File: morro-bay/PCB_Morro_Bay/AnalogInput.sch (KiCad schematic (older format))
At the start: 117 parts, among them SW1 SW_DIP_x10, SW2 SW_DIP_x10, U10 LM2902, U11 LM2902, U12 LM2902, U5 LM2902, U6 LM2902, U7 LM2902, U8 LM2902, U9 LM2902

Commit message: Even more BOM and footprints
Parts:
- added C32, C66: 22uF, Capacitor_SMD:C_0805_2012Metric_Pad1.15x1.40mm_HandSolder, symbol Device:C
- R10, R12, R14, R16, R22, R24, R26, R28, R34, R36, R38, R40, R46, R48, R50, R52, R58, R60, R64, R66: footprint (none) -> Resistor_SMD:R_0603_1608Metric_Pad1.05x0.95mm_HandSolder; Digikey (none) -> https://www.digikey.ca/product-detail/en/panasonic-electron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; Part Number (none) -> ERJ-PB3B1003V
- R11, R13, R15, R21, R23, R25, R27, R33, R35, R9: footprint (none) -> Resistor_SMD:R_0603_1608Metric_Pad1.05x0.95mm_HandSolder; Digikey (none) -> https://www.digikey.ca/product-detail/en/panasonic-electron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; Part Number (none) -> ERJ-PB3B5112V
- R17, R18, R19, R20, R29, R30, R31, R32, R41, R42, R43, R44, R53, R54, R55, R56, R61, R62, R67, R68: value 500 -> 470; footprint (none) -> Resistor_SMD:R_0603_1608Metric_Pad1.05x0.95mm_HandSolder; Digikey (none) -> https://www.digikey.ca/product-detail/en/stackpole-electron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; Part Number (none) -> RMCF0603FT470R
- R37, R39, R45, R47: value 205K -> 51.1K; footprint (none) -> Resistor_SMD:R_0603_1608Metric_Pad1.05x0.95mm_HandSolder; Digikey (none) -> https://www.digikey.ca/product-detail/en/panasonic-electron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; Part Number (none) -> ERJ-PB3B5112V
- R49, R51: footprint (none) -> Resistor_SMD:R_0603_1608Metric_Pad1.05x0.95mm_HandSolder; Digikey (none) -> https://www.digikey.ca/product-detail/en/panasonic-electron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; Part Number (none) -> ERA-3AEB2053V
- R57, R59, R63, R65: value 51.1K -> 205K; footprint (none) -> Resistor_SMD:R_0603_1608Metric_Pad1.05x0.95mm_HandSolder; Digikey (none) -> https://www.digikey.ca/product-detail/en/panasonic-electron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; Part Number (none) -> ERA-3AEB2053V
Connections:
- net 5V_IN_15 is gone; now on net 10V_IN_1: SW2.5
- net 5V_IN_16 is gone; now on net 10V_IN_2: SW2.6
- net 5V_IN_17 is gone; now on net 10V_IN_3: R57.1, SW2.7
- net 5V_IN_20 is gone; now on net 10V_IN_6: R65.1, SW2.10
- net 10V_IN_1: now also R49.1; no longer R37.1
- net 10V_IN_2: now also R51.1; no longer R39.1
- net 10V_IN_3: no longer R45.1
- net 10V_IN_4: now also R59.1, SW2.8; no longer R47.1
- net 10V_IN_5: now also R63.1, SW2.9; no longer R49.1
- net 10V_IN_6: no longer R51.1
- net 3V3_IN_18: now also R59.2, R60.1; no longer R63.2, R64.1
- net 3V3_IN_19: now also R63.2, R64.1; no longer R59.2, R60.1
- net 5V_IN_11: now also R37.1
- net 5V_IN_12: now also R39.1
- net 5V_IN_13: now also R45.1
- net 5V_IN_14: now also R47.1
- net GND: now also C32.2, C66.2
- net IN_18_BUFFERED: now also R62.2; no longer R67.2
- net IN_19_BUFFERED: now also R67.2; no longer R62.2
- net SAMD_ADC_18: now also R62.1; no longer R67.1
- net SAMD_ADC_19: now also R67.1; no longer R62.1
- removed net 5V_IN_18: R63.1, SW2.8
- removed net 5V_IN_19: R59.1, SW2.9
- new net +3V3: C32.1, C66.1
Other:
- moved on the sheet: C40, C41

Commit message: BOM BOM BOM BOM baBOM BOM baBOM...
(Imperial march)
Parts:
- SW1, SW2: footprint (none) -> Button_Switch_SMD:SW_DIP_SPSTx10_Slide_6.7x26.96mm_W8.61mm_P2.54mm_LowProfile; Digikey (none) -> https://www.digikey.ca/product-detail/en/cui-devices/DS04-2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; Part Number (none) -> DS04-254-2-10BK-SMT
- U5, U6, U7, U8, U9: footprint (none) -> Package_SO:SOIC-14_3.9x8.7mm_P1.27mm
- U5, U6, U7, U8, U9: footprint (none) -> Package_SO:SOIC-14_3.9x8.7mm_P1.27mm; Digikey (none) -> https://www.digikey.ca/product-detail/en/texas-instruments/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; Part Number (none) -> LM2902LVIDR
- U9: renamed from U11; footprint (none) -> Package_SO:SOIC-14_3.9x8.7mm_P1.27mm
- U9: renamed from U10; footprint (none) -> Package_SO:SOIC-14_3.9x8.7mm_P1.27mm
- U9: renamed from U12; footprint (none) -> Package_SO:SOIC-14_3.9x8.7mm_P1.27mm
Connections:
- net 3V3_IN_18: now also U9.5 (+); no longer U9.3 (+)
- net 3V3_IN_19: now also U9.10 (+); no longer U9.3 (+)
- net 3V3_IN_20: now also U9.12 (+); no longer U9.3 (+)
- net IN_18_BUFFERED: now also U9.6 (-), U9.7; no longer U9.1, U9.2 (-)
- net IN_19_BUFFERED: now also U9.8, U9.9 (-); no longer U9.1, U9.2 (-)
- net IN_20_BUFFERED: now also U9.13 (-), U9.14; no longer U9.1, U9.2 (-)

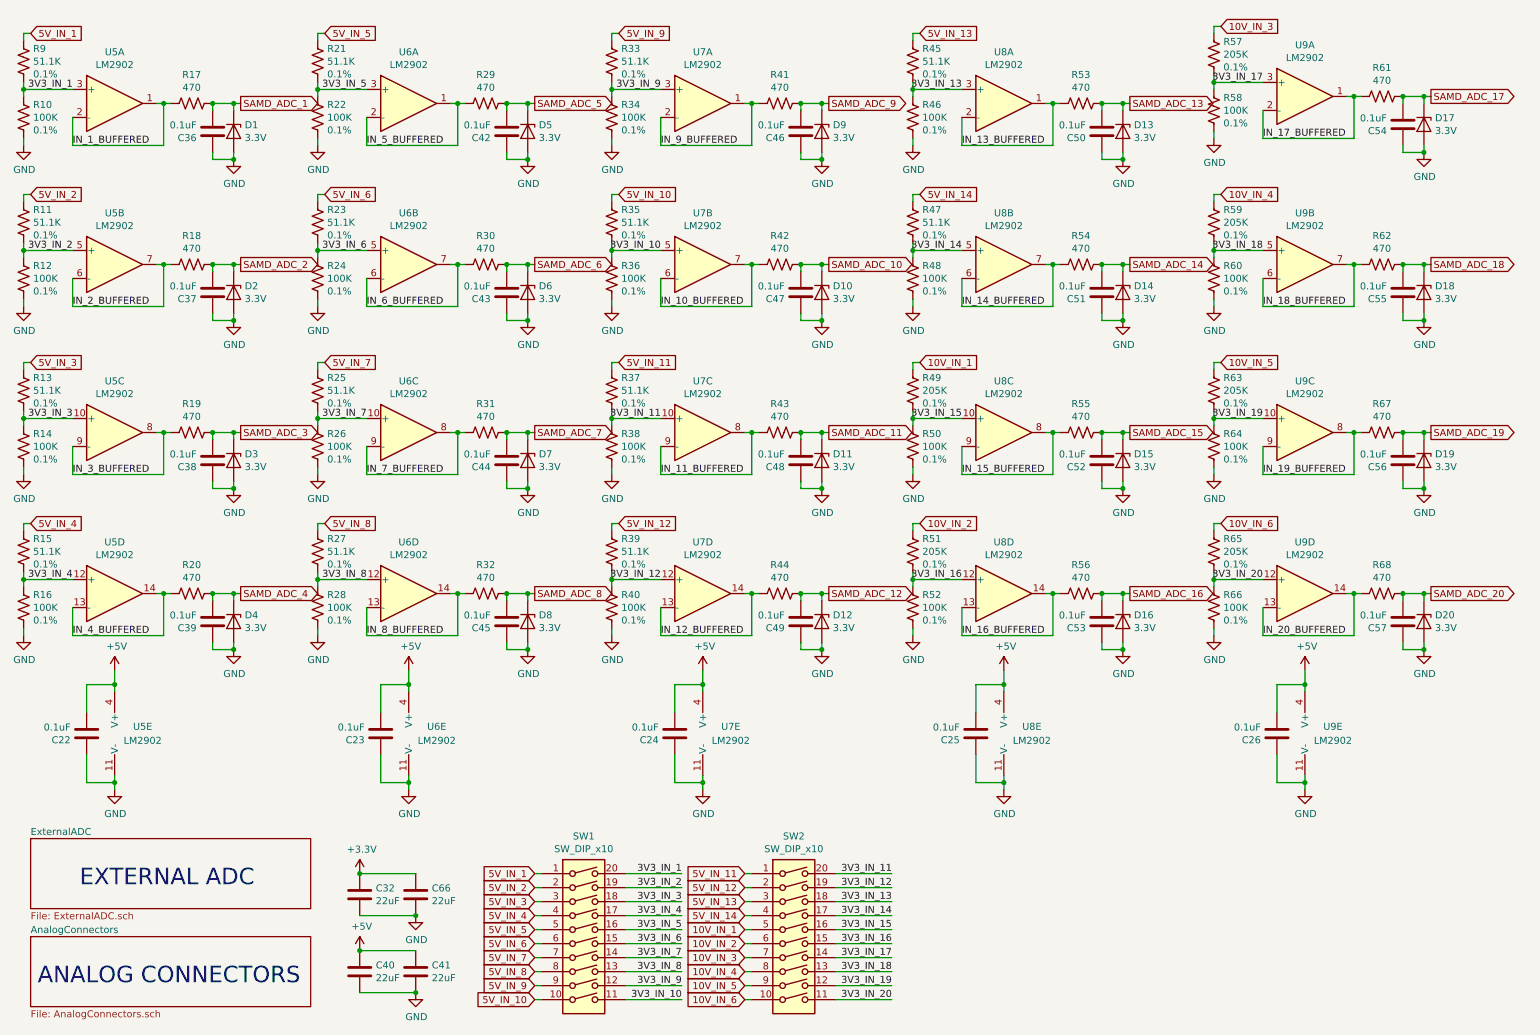
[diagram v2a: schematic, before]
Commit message: Start layout, finish BOM
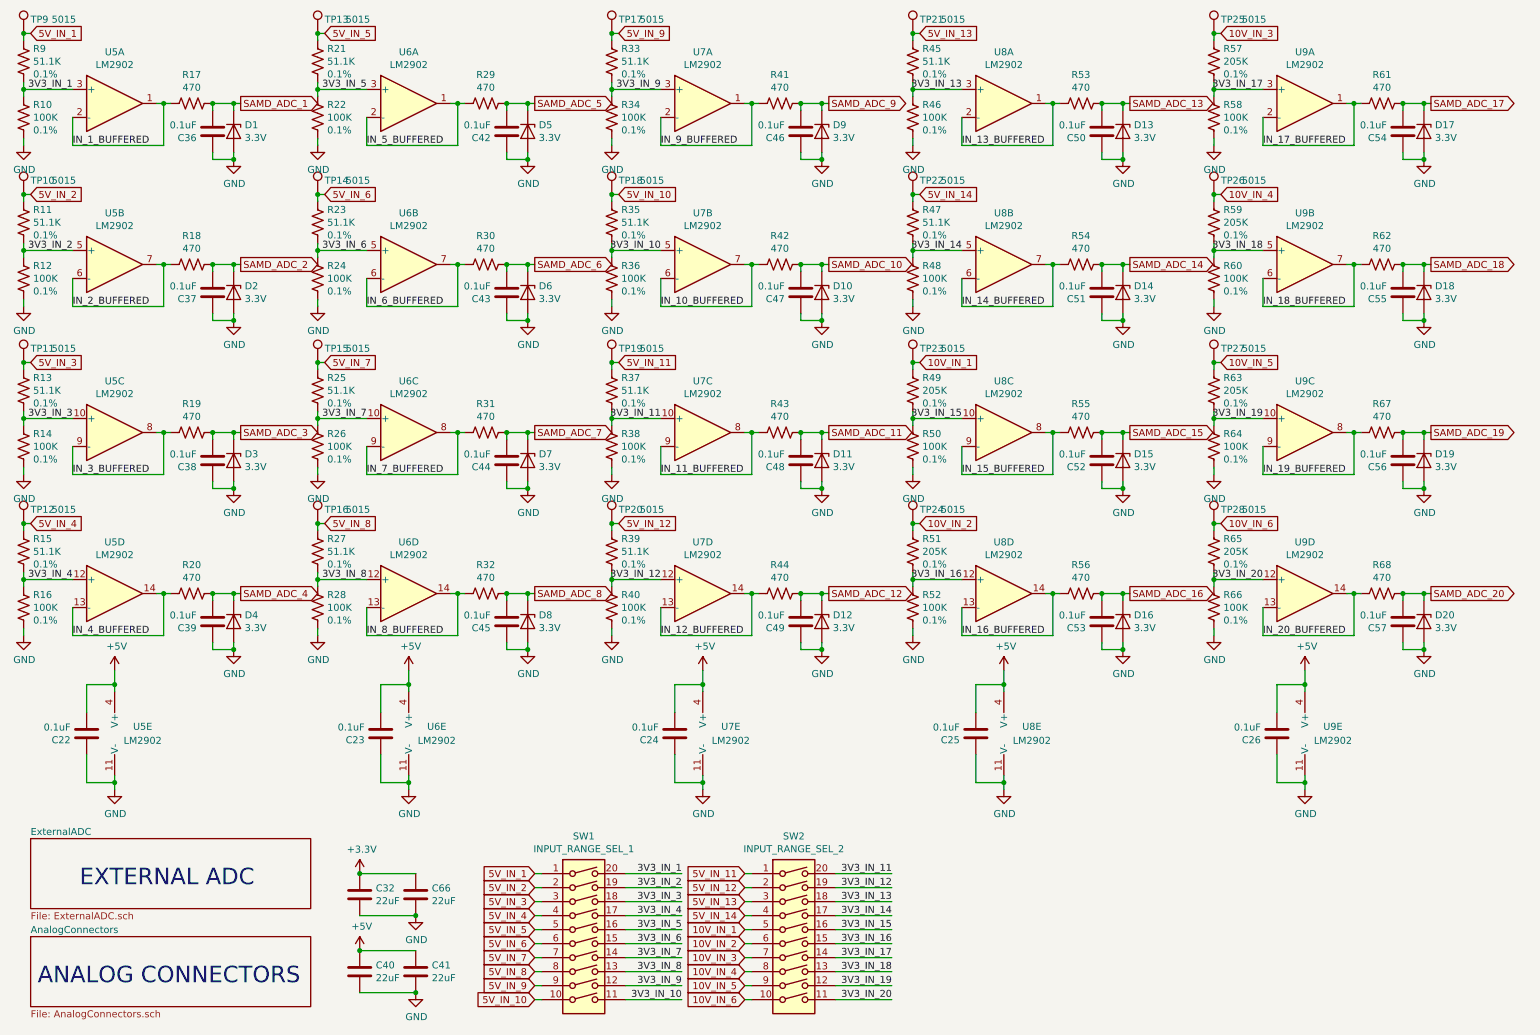
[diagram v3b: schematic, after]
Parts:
- added TP10, TP11, TP12, TP13, TP14, TP15, TP16, TP17, TP18, TP19, TP20, TP21, TP22, TP23, TP24, TP25, TP26, TP27, TP28, TP9: 5015, TestPoint:TestPoint_Keystone_5015_Micro-Minature, symbol Connector:TestPoint
- SW1: value SW_DIP_x10 -> INPUT_RANGE_SEL_1
- SW2: value SW_DIP_x10 -> INPUT_RANGE_SEL_2
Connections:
- net 10V_IN_1: now also TP23.1
- net 10V_IN_2: now also TP24.1
- net 10V_IN_3: now also TP25.1
- net 10V_IN_4: now also TP26.1
- net 10V_IN_5: now also TP27.1
- net 10V_IN_6: now also TP28.1
- net 5V_IN_1: now also TP9.1
- net 5V_IN_10: now also TP18.1
- net 5V_IN_11: now also TP19.1
- net 5V_IN_12: now also TP20.1
- net 5V_IN_13: now also TP21.1
- net 5V_IN_14: now also TP22.1
- net 5V_IN_2: now also TP10.1
- net 5V_IN_3: now also TP11.1
- net 5V_IN_4: now also TP12.1
- net 5V_IN_5: now also TP13.1
- net 5V_IN_6: now also TP14.1
- net 5V_IN_7: now also TP15.1
- net 5V_IN_8: now also TP16.1
- net 5V_IN_9: now also TP17.1
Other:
- moved on the sheet: C54, D17, R57, R58, R61, U9A

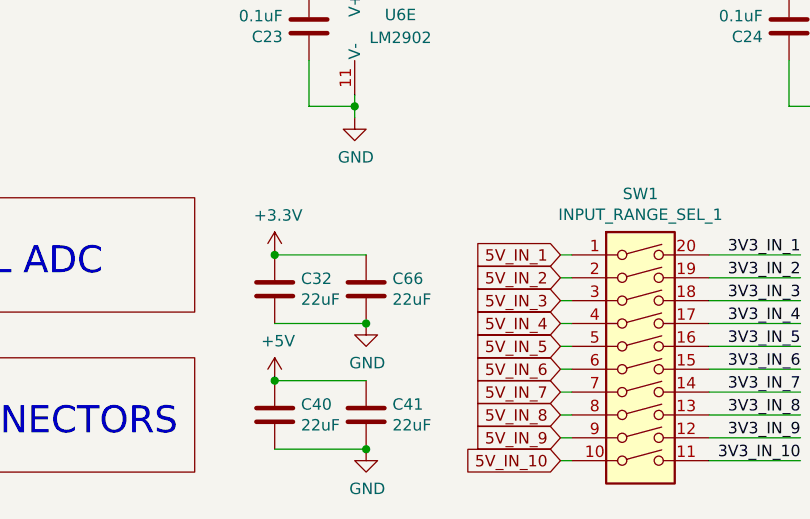
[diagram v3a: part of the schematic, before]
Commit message: Fix values of C7 and C8
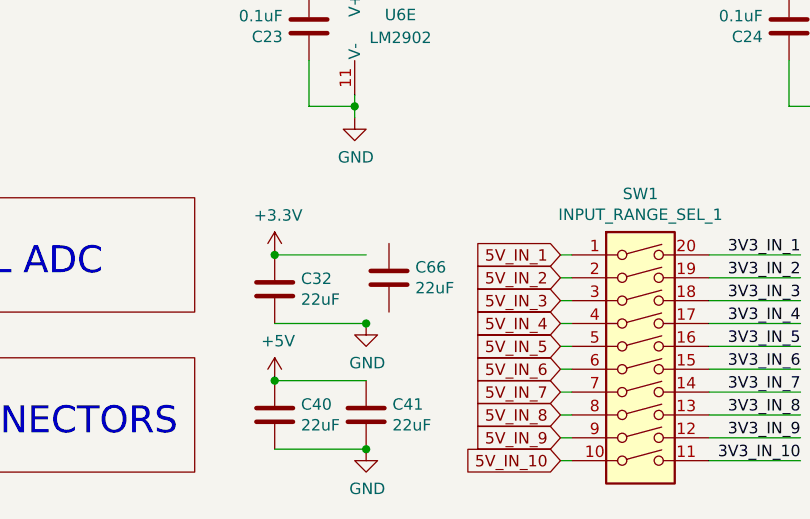
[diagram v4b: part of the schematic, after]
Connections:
- net +3V3: no longer C66.1
- net GND: no longer C66.2
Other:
- moved on the sheet: C66
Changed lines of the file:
@@
 L Device:C C?
 U 1 1 5E88C60F
-P 3400 6800
+P 3500 6750
 AR Path="/5E88C60F" Ref="C?"  Part="1"
 AR Path="/5E59A680/5E88C60F" Ref="C66"  Part="1"
-F 0 "C66" H 3515 6846 50  0000 L CNN
-F 1 "22uF" H 3515 6755 50  0000 L CNN
-F 2 "Capacitor_SMD:C_0805_2012Metric_Pad1.15x1.40mm_HandSolder" H 3438 6650 50  0001 C CNN
-F 3 "~" H 3400 6800 50  0001 C CNN
-F 4 "CL21A226MAQNNNE" H 3400 6800 50  0001 C CNN "Part Number"
-F 5 "https://www.digikey.ca/product-detail/en/samsung-electro-mechanics/CL21A226MAQNNNE/1276-2908-1-ND/3890994" H 3400 6800 50  0001 C CNN "Digikey"
-	1    3400 6800
+F 0 "C66" H 3615 6796 50  0000 L CNN
+F 1 "22uF" H 3615 6705 50  0000 L CNN
+F 2 "Capacitor_SMD:C_0805_2012Metric_Pad1.15x1.40mm_HandSolder" H 3538 6600 50  0001 C CNN
+F 3 "~" H 3500 6750 50  0001 C CNN
+F 4 "CL21A226MAQNNNE" H 3500 6750 50  0001 C CNN "Part Number"
+F 5 "https://www.digikey.ca/product-detail/en/samsung-electro-mechanics/CL21A226MAQNNNE/1276-2908-1-ND/3890994" H 3500 6750 50  0001 C CNN "Digikey"
+	1    3500 6750
 	1    0    0    -1
 $EndComp

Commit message: Start routing
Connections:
- net +3V3: now also C66.1
- net GND: now also C66.2
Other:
- moved on the sheet: C66
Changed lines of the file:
@@
 Wire Wire Line
 	3000 6950 3400 6950
-Connection ~ 3400 6950
 $Comp
 L Device:C C?
@@
 L Device:C C?
 U 1 1 5E88C60F
-P 3500 6750
+P 3400 6800
 AR Path="/5E88C60F" Ref="C?"  Part="1"
 AR Path="/5E59A680/5E88C60F" Ref="C66"  Part="1"
-F 0 "C66" H 3615 6796 50  0000 L CNN
-F 1 "22uF" H 3615 6705 50  0000 L CNN
-F 2 "Capacitor_SMD:C_0805_2012Metric_Pad1.15x1.40mm_HandSolder" H 3538 6600 50  0001 C CNN
-F 3 "~" H 3500 6750 50  0001 C CNN
-F 4 "CL21A226MAQNNNE" H 3500 6750 50  0001 C CNN "Part Number"
-F 5 "https://www.digikey.ca/product-detail/en/samsung-electro-mechanics/CL21A226MAQNNNE/1276-2908-1-ND/3890994" H 3500 6750 50  0001 C CNN "Digikey"
-	1    3500 6750
+F 0 "C66" H 3515 6846 50  0000 L CNN
+F 1 "22uF" H 3515 6755 50  0000 L CNN
+F 2 "Capacitor_SMD:C_0805_2012Metric_Pad1.15x1.40mm_HandSolder" H 3438 6650 50  0001 C CNN
+F 3 "~" H 3400 6800 50  0001 C CNN
+F 4 "CL21A226MAQNNNE" H 3400 6800 50  0001 C CNN "Part Number"
+F 5 "https://www.digikey.ca/product-detail/en/samsung-electro-mechanics/CL21A226MAQNNNE/1276-2908-1-ND/3890994" H 3400 6800 50  0001 C CNN "Digikey"
+	1    3400 6800
 	1    0    0    -1
 $EndComp
@@
 Connection ~ 6950 1800
 Connection ~ 9100 1800
+Connection ~ 3400 6950
 $EndSCHEMATC

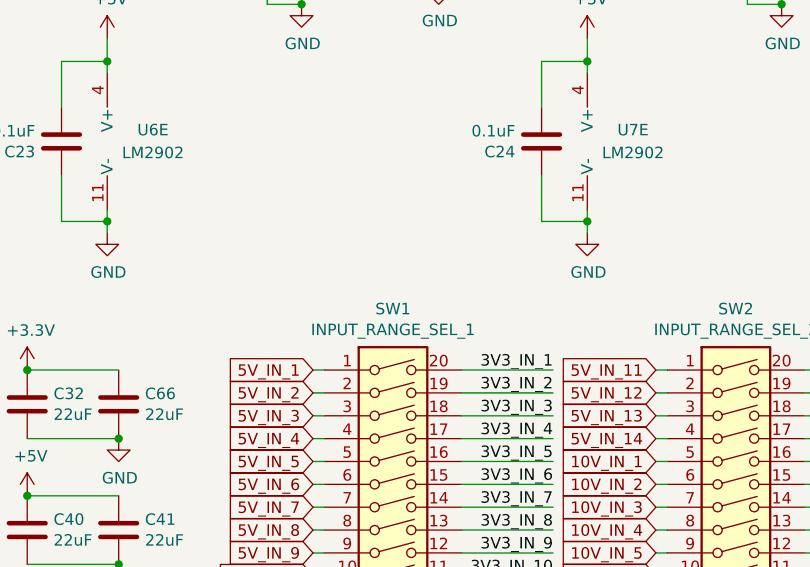
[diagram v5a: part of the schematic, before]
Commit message: Add direction silkscreen for DIP switches
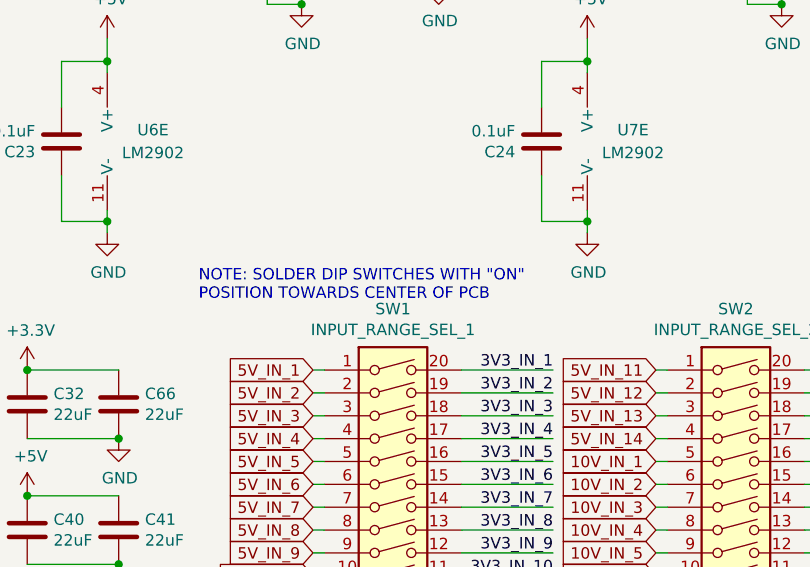
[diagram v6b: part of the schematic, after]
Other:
- note added: "NOTE: SOLDER DIP SWITCHES WITH "ON"\nPOSITION TOWARDS CENTER OF PCB"
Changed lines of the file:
@@
 Connection ~ 9100 1800
 Connection ~ 3400 6950
+Text Notes 3750 6350 0    50   ~ 0
+NOTE: SOLDER DIP SWITCHES WITH "ON"\nPOSITION TOWARDS CENTER OF PCB
 $EndSCHEMATC

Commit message: Export final gerbers for MB
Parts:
- C32, C40, C41, C66: Digikey https://www.digikey.ca/product-detail/en/samsung-electro-me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 -> https://www.digikey.ca/en/products/detail/yageo/CC0805MKX5R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; Part Number CL21A226MAQNNNE -> CC0805MKX5R8BB226
- R10, R12, R14, R16, R22, R24, R26, R28, R34, R36, R38, R40, R46, R48, R50, R52, R58, R60, R64, R66: Digikey https://www.digikey.ca/product-detail/en/panasonic-electron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 -> https://www.digikey.ca/en/products/detail/panasonic-electro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; Part Number ERJ-PB3B1003V -> ERA-3AEB104V
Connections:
- net +3V3: no longer C32.1
- net GND: no longer C32.2
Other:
- moved on the sheet: C32
